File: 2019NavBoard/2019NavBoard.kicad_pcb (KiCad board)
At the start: 2 copper layers, 61 x 88.7 mm, 23 parts, among them J1 Conn_Coaxial, U5 FGPMMOPA6H

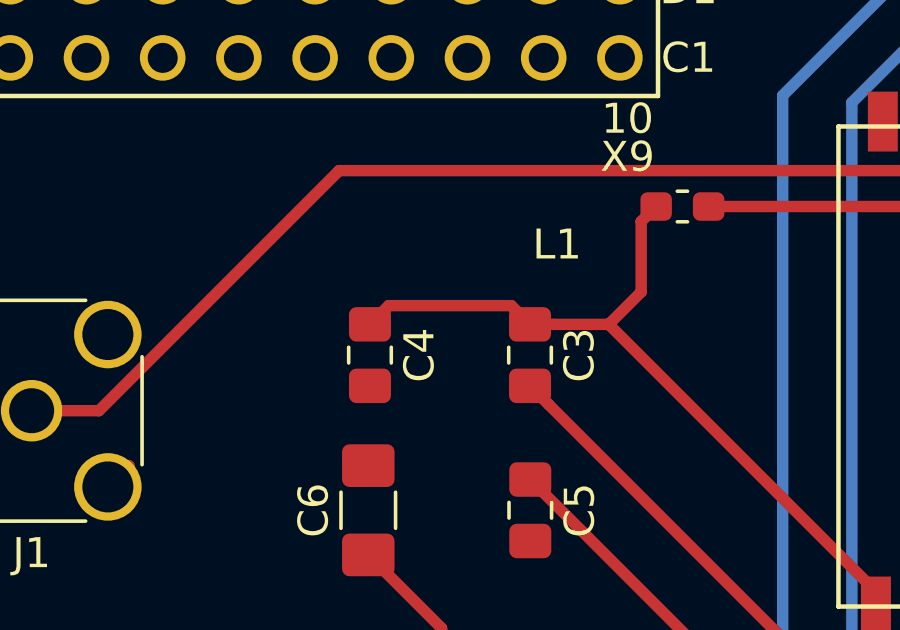
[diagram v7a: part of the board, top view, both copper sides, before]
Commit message: Slight changes to PCB traces
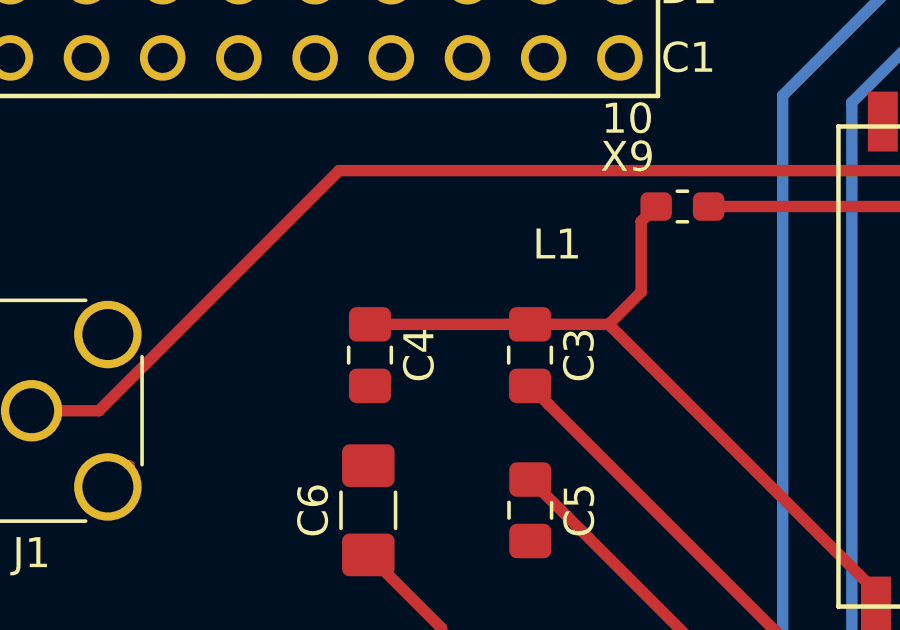
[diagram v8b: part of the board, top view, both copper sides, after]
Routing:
- net Net-(C3-Pad1): track 26.2 -> 25.7 mm
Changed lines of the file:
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@@
     (thickness 1.6)
     (drawings 27)
-    (tracks 121)
+    (tracks 120)
     (zones 0)
     (modules 23)
@@
   (segment (start 134.5438 93.4313) (end 132.1 90.9875) (width 0.381) (layer F.Cu) (net 2))
   (segment (start 143.3459 99.4674) (end 147.066 103.1875) (width 0.381) (layer F.Cu) (net 2))
-  (segment (start 134.5438 99.4674) (end 143.3459 99.4674) (width 0.381) (layer F.Cu) (net 2))
   (segment (start 134.5438 99.4674) (end 134.5438 93.4313) (width 0.381) (layer F.Cu) (net 2))
+  (segment (start 134.5438 99.4674) (end 143.3459 99.4674) (width 0.381) (layer F.Cu) (net 2))
   (segment (start 137.5386 83.303) (end 137.4902 83.303) (width 0.381) (layer F.Cu) (net 3))
-  (segment (start 132.779572 82.679628) (end 132.1562 83.303) (width 0.381) (layer F.Cu) (net 3))
-  (segment (start 136.866828 82.679628) (end 132.779572 82.679628) (width 0.381) (layer F.Cu) (net 3))
-  (segment (start 137.4902 83.303) (end 136.866828 82.679628) (width 0.381) (layer F.Cu) (net 3))
   (segment (start 138.2902 83.303) (end 137.4902 83.303) (width 0.381) (layer F.Cu) (net 3))
   (segment (start 140.1148 83.303) (end 138.2902 83.303) (width 0.381) (layer F.Cu) (net 3))
-  (segment (start 149.0218 92.21) (end 140.1148 83.303) (width 0.381) (layer F.Cu) (net 3))
   (segment (start 149.0218 92.71) (end 149.0218 92.21) (width 0.381) (layer F.Cu) (net 3))
   (segment (start 141.196128 82.221672) (end 140.1148 83.303) (width 0.381) (layer F.Cu) (net 3))
   (segment (start 141.196128 79.874072) (end 141.196128 82.221672) (width 0.381) (layer F.Cu) (net 3))
   (segment (start 141.6952 79.375) (end 141.196128 79.874072) (width 0.381) (layer F.Cu) (net 3))
+  (segment (start 136.6902 83.303) (end 132.1562 83.303) (width 0.381) (layer F.Cu) (net 3))
+  (segment (start 137.4902 83.303) (end 136.6902 83.303) (width 0.381) (layer F.Cu) (net 3))
+  (segment (start 149.0218 92.21) (end 140.1148 83.303) (width 0.381) (layer F.Cu) (net 3))
   (segment (start 137.5 88.475) (end 144.1988 95.1738) (width 0.381) (layer F.Cu) (net 4))
   (segment (start 153.5218 94.091) (end 153.5218 92.71) (width 0.381) (layer F.Cu) (net 4))
@@
   (segment (start 164.1348 75.5904) (end 157.607 69.0626) (width 0.381) (layer F.Cu) (net 9))
   (segment (start 164.1348 77.363876) (end 164.1348 75.5904) (width 0.381) (layer F.Cu) (net 9))
-  (segment (start 143.4452 79.375) (end 162.123676 79.375) (width 0.381) (layer F.Cu) (net 9))
   (segment (start 162.123676 79.375) (end 164.1348 77.363876) (width 0.381) (layer F.Cu) (net 9))
   (segment (start 162.123676 81.146224) (end 162.123676 79.375) (width 0.381) (layer F.Cu) (net 9))
   (segment (start 169.412592 88.43514) (end 162.123676 81.146224) (width 0.381) (layer F.Cu) (net 9))
+  (segment (start 143.4452 79.375) (end 162.123676 79.375) (width 0.381) (layer F.Cu) (net 9))
   (segment (start 169.4778 93.3868) (end 169.418 93.4466) (width 0.381) (layer F.Cu) (net 10))
   (segment (start 172.847 93.3868) (end 169.4778 93.3868) (width 0.381) (layer F.Cu) (net 10))
@@
   (segment (start 175.133 70.3834) (end 173.7868 69.0372) (width 0.381) (layer F.Cu) (net 48))
   (segment (start 175.133 77.2414) (end 175.133 70.3834) (width 0.381) (layer F.Cu) (net 48))
-  (segment (start 174.361653 78.012747) (end 175.133 77.2414) (width 0.381) (layer F.Cu) (net 48))
   (segment (start 152.146 99.7585) (end 152.3365 99.568) (width 0.381) (layer F.Cu) (net 48))
   (segment (start 152.146 103.1875) (end 152.146 99.7585) (width 0.381) (layer F.Cu) (net 48))
@@
   (segment (start 145.1229 110.2106) (end 140.5382 110.2106) (width 0.381) (layer F.Cu) (net 48))
   (via (at 153.8478 97.2312) (size 0.8) (drill 0.4) (layers F.Cu B.Cu) (net 48))
-  (segment (start 165.9038 76.2508) (end 165.8276 76.1746) (width 0.381) (layer F.Cu) (net 48))
-  (segment (start 165.9038 80.391) (end 165.9038 76.2508) (width 0.381) (layer F.Cu) (net 48))
-  (segment (start 167.665747 78.012747) (end 165.8276 76.1746) (width 0.381) (layer F.Cu) (net 48))
-  (segment (start 174.361653 78.012747) (end 167.665747 78.012747) (width 0.381) (layer F.Cu) (net 48))
   (segment (start 126.6365 116.211502) (end 126.6365 113.9015) (width 0.381) (layer F.Cu) (net 48))
   (segment (start 125.247001 117.601001) (end 126.6365 116.211502) (width 0.381) (layer F.Cu) (net 48))
@@
   (segment (start 118.777502 116.211502) (end 118.777502 117.914244) (width 0.381) (layer F.Cu) (net 48))
   (segment (start 117.627001 115.061001) (end 118.777502 116.211502) (width 0.381) (layer F.Cu) (net 48))
+  (segment (start 165.9038 76.2508) (end 165.8276 76.1746) (width 0.381) (layer F.Cu) (net 48))
+  (segment (start 165.9038 80.391) (end 165.9038 76.2508) (width 0.381) (layer F.Cu) (net 48))
+  (segment (start 167.665747 78.012747) (end 165.8276 76.1746) (width 0.381) (layer F.Cu) (net 48))
+  (segment (start 174.361653 78.012747) (end 175.133 77.2414) (width 0.381) (layer F.Cu) (net 48))
+  (segment (start 174.361653 78.012747) (end 167.665747 78.012747) (width 0.381) (layer F.Cu) (net 48))
   (segment (start 167.8776 69.8664) (end 168.7068 69.0372) (width 0.381) (layer F.Cu) (net 49))
   (segment (start 167.8776 76.1746) (end 167.8776 69.8664) (width 0.381) (layer F.Cu) (net 49))
